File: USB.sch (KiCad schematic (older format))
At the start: 8 parts, among them IC5 ADuM4160

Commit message: - corrected current filter resistors - adapted USB footprint - added 0.1% note to dc bus voltage divider
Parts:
- IC5: symbol Auktoralib:ADuM4160 -> HSWR-V2-rescue:ADuM4160-Auktoralib
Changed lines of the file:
@@
 $EndDescr
 $Comp
-L Auktoralib:ADuM4160 IC5
+L HSWR-V2-rescue:ADuM4160-Auktoralib IC5
 U 1 1 5CA151F5
 P 5450 3900

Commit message: - rescued schematic - added *.sch-bak to ignore - fixed bypass diode polarity - fixed PDEN being low - added 0R resistors instead of USB iso option - added caps to DCDC - added filter to VDDA
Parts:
- added R50, R51: 0R, Resistor_SMD:R_0805_2012Metric, symbol HSWR-V2-rescue:R-Device
- C10, C39, C40: symbol Device:C -> HSWR-V2-rescue:C-Device
- IC5: symbol HSWR-V2-rescue:ADuM4160-Auktoralib -> Interface_USB:ADUM4160
- R31, R41, R42, R43: symbol Device:R -> HSWR-V2-rescue:R-Device
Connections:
- wire segments 24 -> 34
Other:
- moved on the sheet: C10, C39, C40, R31, R41, R42, R43

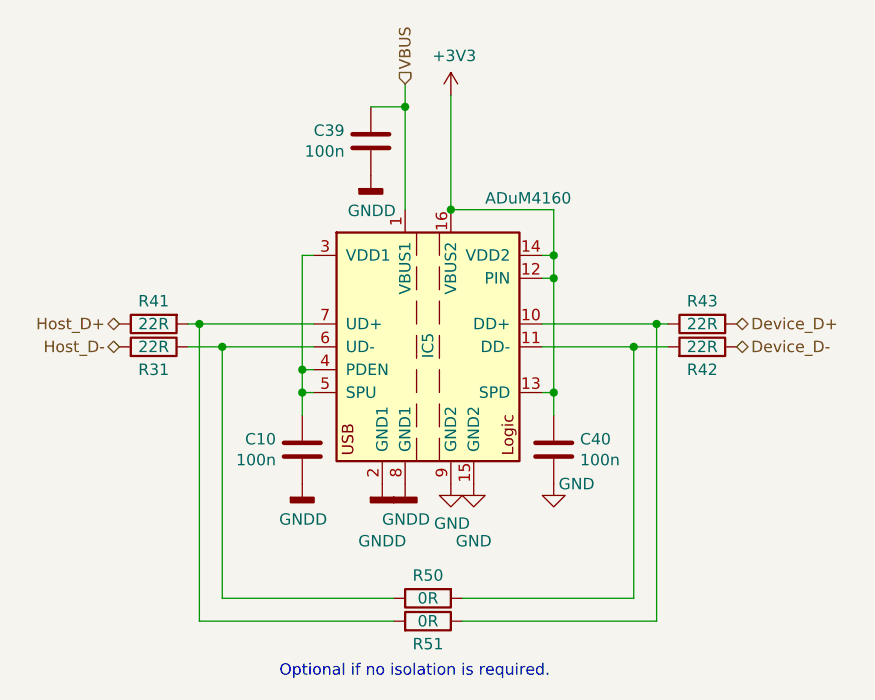
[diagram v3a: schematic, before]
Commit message: - changed CSA for Hall effect sensors - updated power stage layout
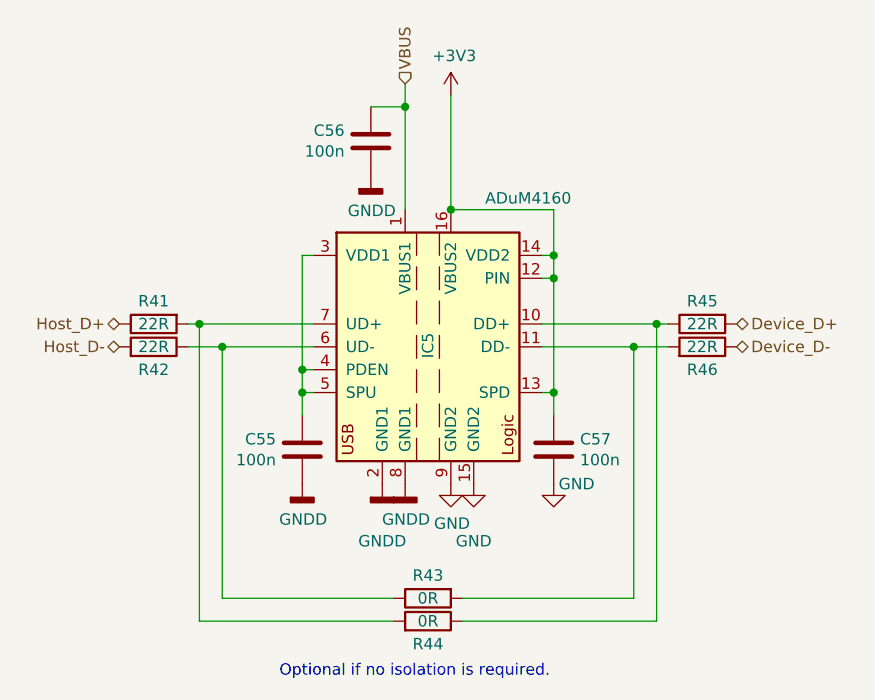
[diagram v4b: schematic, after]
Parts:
- renumbered C10 to C55, C39 to C56, C40 to C57, R31 to R42, R50 to R43, R51 to R44, R43 to R45, R42 to R46
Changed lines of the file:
@@
 $EndDescr
 $Comp
-L HSWR-V2-rescue:C-Device C10
+L HSWR-V2-rescue:C-Device C55
 U 1 1 5CA1534B
 P 5150 4200
-F 0 "C10" H 5035 4154 50  0000 R CNN
+F 0 "C55" H 5035 4154 50  0000 R CNN
 F 1 "100n" H 5035 4245 50  0000 R CNN
 F 2 "Capacitor_SMD:C_0805_2012Metric" H 5188 4050 50  0001 C CNN
@@
 $EndComp
 $Comp
-L HSWR-V2-rescue:C-Device C39
+L HSWR-V2-rescue:C-Device C56
 U 1 1 5CA1544F
 P 5450 2850
-F 0 "C39" H 5335 2804 50  0000 R CNN
+F 0 "C56" H 5335 2804 50  0000 R CNN
 F 1 "100n" H 5335 2895 50  0000 R CNN
 F 2 "Capacitor_SMD:C_0805_2012Metric" H 5488 2700 50  0001 C CNN
@@
 VBUS
 $Comp
-L HSWR-V2-rescue:C-Device C40
+L HSWR-V2-rescue:C-Device C57
 U 1 1 5CA15529
 P 6250 4200
-F 0 "C40" H 6135 4154 50  0000 R CNN
+F 0 "C57" H 6135 4154 50  0000 R CNN
 F 1 "100n" H 6135 4245 50  0000 R CNN
 F 2 "Capacitor_SMD:C_0805_2012Metric" H 6288 4050 50  0001 C CNN
@@
 $EndComp
 $Comp
-L HSWR-V2-rescue:GND-power #PWR0175
+L HSWR-V2-rescue:GND-power #PWR0118
 U 1 1 5CA155CB
 P 6250 4350
-F 0 "#PWR0175" H 6250 4100 50  0001 C CNN
+F 0 "#PWR0118" H 6250 4100 50  0001 C CNN
 F 1 "GND" H 6350 4350 50  0000 C CNN
 F 2 "" H 6250 4350 50  0001 C CNN
@@
 $EndComp
 $Comp
-L HSWR-V2-rescue:+3V3-power #PWR0176
+L HSWR-V2-rescue:+3V3-power #PWR0115
 U 1 1 5CA1568C
 P 5800 2650
-F 0 "#PWR0176" H 5800 2500 50  0001 C CNN
+F 0 "#PWR0115" H 5800 2500 50  0001 C CNN
 F 1 "+3V3" H 5815 2823 50  0000 C CNN
 F 2 "" H 5800 2650 50  0001 C CNN
@@
 $EndComp
 $Comp
-L HSWR-V2-rescue:GND-power #PWR0179
+L HSWR-V2-rescue:GND-power #PWR0117
 U 1 1 5CA15B5B
 P 5900 4350
-F 0 "#PWR0179" H 5900 4100 50  0001 C CNN
+F 0 "#PWR0117" H 5900 4100 50  0001 C CNN
 F 1 "GND" H 5900 4100 50  0000 C CNN
 F 2 "" H 5900 4350 50  0001 C CNN
@@
 $EndComp
 $Comp
-L HSWR-V2-rescue:GND-power #PWR0180
+L HSWR-V2-rescue:GND-power #PWR0116
 U 1 1 5CA15B75
 P 5800 4350
-F 0 "#PWR0180" H 5800 4100 50  0001 C CNN
+F 0 "#PWR0116" H 5800 4100 50  0001 C CNN
 F 1 "GND" H 5805 4177 50  0000 C CNN
 F 2 "" H 5800 4350 50  0001 C CNN
@@
 Device_D+
 $Comp
-L HSWR-V2-rescue:R-Device R31
+L HSWR-V2-rescue:R-Device R42
 U 1 1 5CA2CFC2
 P 4500 3750
-F 0 "R31" V 4400 3750 50  0000 C CNN
+F 0 "R42" V 4400 3750 50  0000 C CNN
 F 1 "22R" V 4500 3750 50  0000 C CNN
 F 2 "Resistor_SMD:R_0805_2012Metric" V 4430 3750 50  0001 C CNN
@@
 $EndComp
 $Comp
-L HSWR-V2-rescue:R-Device R42
+L HSWR-V2-rescue:R-Device R46
 U 1 1 5CA2D1EF
 P 6900 3750
-F 0 "R42" V 6800 3750 50  0000 C CNN
+F 0 "R46" V 6800 3750 50  0000 C CNN
 F 1 "22R" V 6900 3750 50  0000 C CNN
 F 2 "Resistor_SMD:R_0805_2012Metric" V 6830 3750 50  0001 C CNN
@@
 $EndComp
 $Comp
-L HSWR-V2-rescue:R-Device R43
+L HSWR-V2-rescue:R-Device R45
 U 1 1 5CA2D21F
 P 6900 3650
-F 0 "R43" V 6800 3650 50  0000 C CNN
+F 0 "R45" V 6800 3650 50  0000 C CNN
 F 1 "22R" V 6900 3650 50  0000 C CNN
 F 2 "Resistor_SMD:R_0805_2012Metric" V 6830 3650 50  0001 C CNN
@@
 $EndComp
 $Comp
-L HSWR-V2-rescue:GNDD-power #PWR0173
+L HSWR-V2-rescue:GNDD-power #PWR0114
 U 1 1 5CA2D72E
 P 5600 4350
-F 0 "#PWR0173" H 5600 4100 50  0001 C CNN
+F 0 "#PWR0114" H 5600 4100 50  0001 C CNN
 F 1 "GNDD" H 5604 4195 50  0000 C CNN
 F 2 "" H 5600 4350 50  0001 C CNN
@@
 $EndComp
 $Comp
-L HSWR-V2-rescue:GNDD-power #PWR0174
+L HSWR-V2-rescue:GNDD-power #PWR0113
 U 1 1 5CA2D7D0
 P 5500 4350
-F 0 "#PWR0174" H 5500 4100 50  0001 C CNN
+F 0 "#PWR0113" H 5500 4100 50  0001 C CNN
 F 1 "GNDD" H 5500 4100 50  0000 C CNN
 F 2 "" H 5500 4350 50  0001 C CNN
@@
 $EndComp
 $Comp
-L HSWR-V2-rescue:GNDD-power #PWR0178
+L HSWR-V2-rescue:GNDD-power #PWR0111
 U 1 1 5CA2D853
 P 5150 4350
-F 0 "#PWR0178" H 5150 4100 50  0001 C CNN
+F 0 "#PWR0111" H 5150 4100 50  0001 C CNN
 F 1 "GNDD" H 5154 4195 50  0000 C CNN
 F 2 "" H 5150 4350 50  0001 C CNN
@@
 $EndComp
 $Comp
-L HSWR-V2-rescue:GNDD-power #PWR0181
+L HSWR-V2-rescue:GNDD-power #PWR0112
 U 1 1 5CA2D86E
 P 5450 3000
-F 0 "#PWR0181" H 5450 2750 50  0001 C CNN
+F 0 "#PWR0112" H 5450 2750 50  0001 C CNN
 F 1 "GNDD" H 5454 2845 50  0000 C CNN
 F 2 "" H 5450 3000 50  0001 C CNN
@@
 Connection ~ 5600 2700
 $Comp
-L HSWR-V2-rescue:R-Device R51
+L HSWR-V2-rescue:R-Device R44
 U 1 1 5E2DF282
 P 5700 4950
-F 0 "R51" V 5600 4950 50  0000 C CNN
+F 0 "R44" V 5600 4950 50  0000 C CNN
 F 1 "0R" V 5700 4950 50  0000 C CNN
 F 2 "Resistor_SMD:R_0805_2012Metric" V 5630 4950 50  0001 C CNN
@@
 $EndComp
 $Comp
-L HSWR-V2-rescue:R-Device R50
+L HSWR-V2-rescue:R-Device R43
 U 1 1 5E2DFF19
 P 5700 4850
-F 0 "R50" V 5600 4850 50  0000 C CNN
+F 0 "R43" V 5600 4850 50  0000 C CNN
 F 1 "0R" V 5700 4850 50  0000 C CNN
 F 2 "Resistor_SMD:R_0805_2012Metric" V 5630 4850 50  0001 C CNN

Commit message: - removed rescue lib and symbols - added HSWR.lib
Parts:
- C55, C56, C57: symbol HSWR-V2-rescue:C-Device -> Device:C
- R41, R42, R43, R44, R45, R46: symbol HSWR-V2-rescue:R-Device -> Device:R
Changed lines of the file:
@@
 $Descr A4 11693 8268
 encoding utf-8
-Sheet 8 8
+Sheet 7 8
 Title ""
 Date ""
@@
 $EndDescr
 $Comp
-L HSWR-V2-rescue:C-Device C55
+L Device:C C55
 U 1 1 5CA1534B
 P 5150 4200
@@
 $EndComp
 $Comp
-L HSWR-V2-rescue:C-Device C56
+L Device:C C56
 U 1 1 5CA1544F
 P 5450 2850
@@
 VBUS
 $Comp
-L HSWR-V2-rescue:C-Device C57
+L Device:C C57
 U 1 1 5CA15529
 P 6250 4200
@@
 $EndComp
 $Comp
-L HSWR-V2-rescue:GND-power #PWR0118
+L power:GND #PWR0118
 U 1 1 5CA155CB
 P 6250 4350
@@
 $EndComp
 $Comp
-L HSWR-V2-rescue:+3V3-power #PWR0115
+L power:+3V3 #PWR0115
 U 1 1 5CA1568C
 P 5800 2650
@@
 $EndComp
 $Comp
-L HSWR-V2-rescue:GND-power #PWR0117
+L power:GND #PWR0117
 U 1 1 5CA15B5B
 P 5900 4350
@@
 $EndComp
 $Comp
-L HSWR-V2-rescue:GND-power #PWR0116
+L power:GND #PWR0116
 U 1 1 5CA15B75
 P 5800 4350
@@
 Device_D+
 $Comp
-L HSWR-V2-rescue:R-Device R42
+L Device:R R42
 U 1 1 5CA2CFC2
 P 4500 3750
@@
 $EndComp
 $Comp
-L HSWR-V2-rescue:R-Device R41
+L Device:R R41
 U 1 1 5CA2D049
 P 4500 3650
@@
 $EndComp
 $Comp
-L HSWR-V2-rescue:R-Device R46
+L Device:R R46
 U 1 1 5CA2D1EF
 P 6900 3750
@@
 $EndComp
 $Comp
-L HSWR-V2-rescue:R-Device R45
+L Device:R R45
 U 1 1 5CA2D21F
 P 6900 3650
@@
 $EndComp
 $Comp
-L HSWR-V2-rescue:GNDD-power #PWR0114
+L power:GNDD #PWR0114
 U 1 1 5CA2D72E
 P 5600 4350
@@
 $EndComp
 $Comp
-L HSWR-V2-rescue:GNDD-power #PWR0113
+L power:GNDD #PWR0113
 U 1 1 5CA2D7D0
 P 5500 4350
@@
 $EndComp
 $Comp
-L HSWR-V2-rescue:GNDD-power #PWR0111
+L power:GNDD #PWR0111
 U 1 1 5CA2D853
 P 5150 4350
@@
 $EndComp
 $Comp
-L HSWR-V2-rescue:GNDD-power #PWR0112
+L power:GNDD #PWR0112
 U 1 1 5CA2D86E
 P 5450 3000
@@
 Connection ~ 5600 2700
 $Comp
-L HSWR-V2-rescue:R-Device R44
+L Device:R R44
 U 1 1 5E2DF282
 P 5700 4950
@@
 $EndComp
 $Comp
-L HSWR-V2-rescue:R-Device R43
+L Device:R R43
 U 1 1 5E2DFF19
 P 5700 4850
